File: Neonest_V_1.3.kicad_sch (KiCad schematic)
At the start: 4 parts

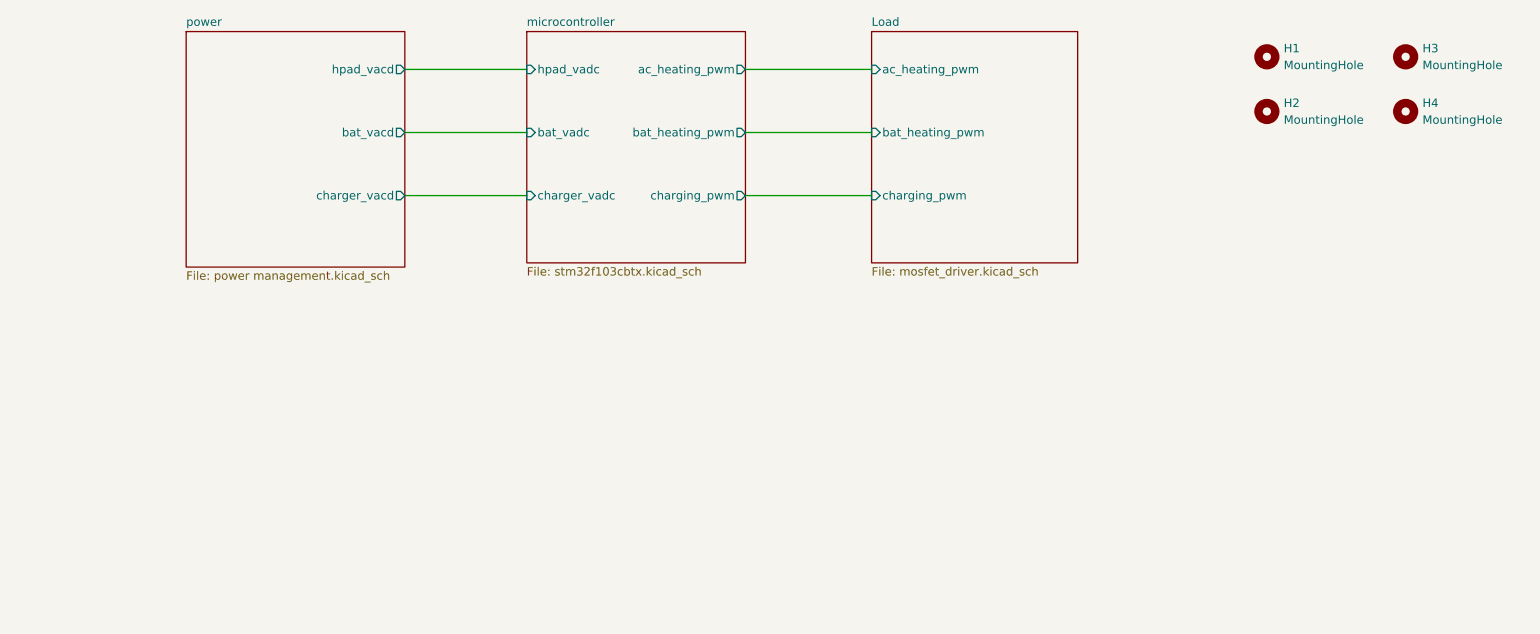
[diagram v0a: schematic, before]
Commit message: Formatted schematic and Increased power tracks
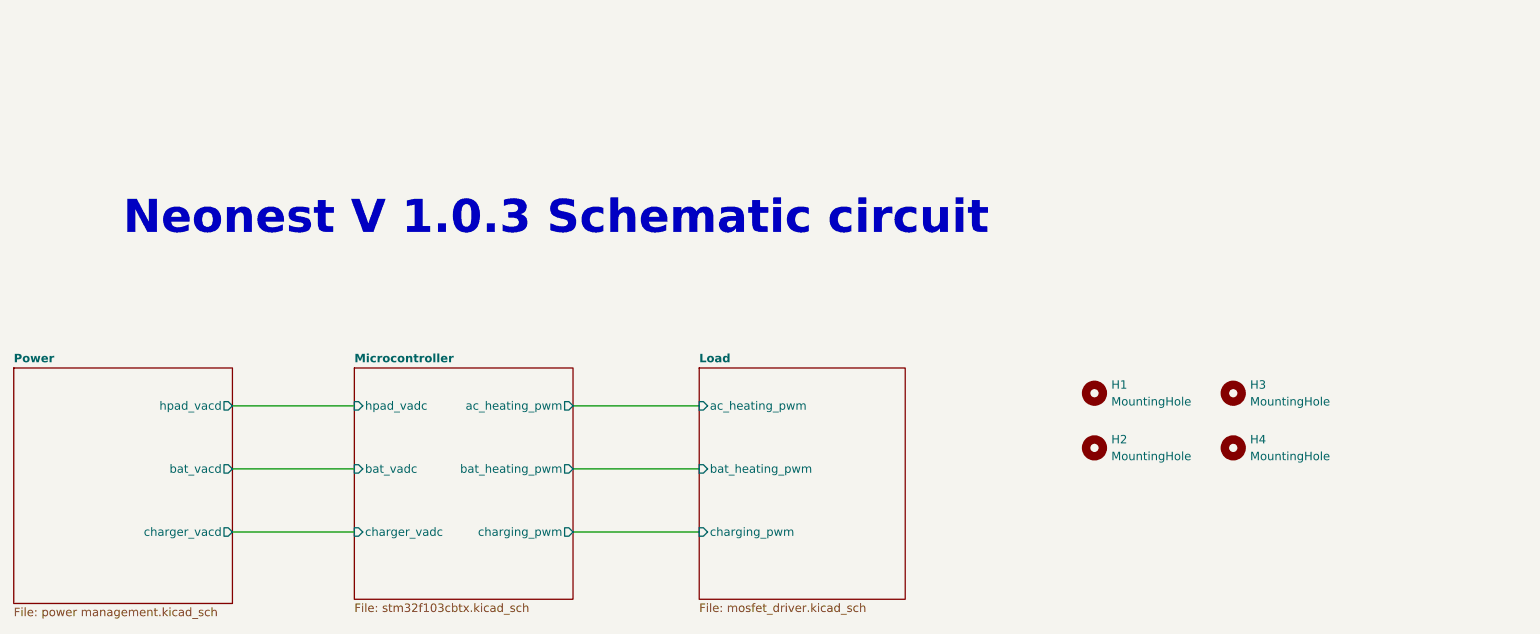
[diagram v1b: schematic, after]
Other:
- sheet microcontroller renamed Microcontroller
- sheet power renamed Power
- note added: "Neonest V 1.0.3 Schematic circuit"
- company: (none) -> Che innovations
- title: (none) -> Neonest v 1.3
- moved on the sheet: H1, H2, H3, H4
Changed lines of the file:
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@@
 (kicad_sch (version 20230121) (generator eeschema)
   (paper "A4")
-  (wire (pts (xy 168.91 43.815) (xy 187.96 43.815))
+  (title_block
+    (title "Neonest v 1.3")
+    (date "2025-08-07")
+    (company "Che innovations")
+  )
+  (wire (pts (xy 142.875 94.615) (xy 161.925 94.615))
     (stroke (width 0) (type default))
   )
-  (wire (pts (xy 117.475 34.29) (xy 135.89 34.29))
+  (wire (pts (xy 91.44 85.09) (xy 109.855 85.09))
     (stroke (width 0) (type default))
   )
-  (wire (pts (xy 117.475 53.34) (xy 135.89 53.34))
+  (wire (pts (xy 91.44 104.14) (xy 109.855 104.14))
     (stroke (width 0) (type default))
   )
-  (wire (pts (xy 168.91 34.29) (xy 187.96 34.29))
+  (wire (pts (xy 142.875 85.09) (xy 161.925 85.09))
     (stroke (width 0) (type default))
   )
-  (wire (pts (xy 168.91 53.34) (xy 187.96 53.34))
+  (wire (pts (xy 142.875 104.14) (xy 161.925 104.14))
     (stroke (width 0) (type default))
   )
-  (wire (pts (xy 117.475 43.815) (xy 135.89 43.815))
+  (wire (pts (xy 91.44 94.615) (xy 109.855 94.615))
     (stroke (width 0) (type default))
   )
-  (symbol (lib_id "Mechanical:MountingHole") (at 268.605 32.385 0) (unit 1)
+  (text "Neonest V 1.0.3 Schematic circuit" (at 74.93 59.69 0)
+    (effects (font (size 5 5) (thickness 1) bold) (justify left bottom))
+  )
+  (symbol (lib_id "Mechanical:MountingHole") (at 242.57 83.185 0) (unit 1)
     (in_bom yes) (on_board yes) (dnp no) (fields_autoplaced)
-    (property "Reference" "H3" (at 271.145 31.115 0)
+    (property "Reference" "H3" (at 245.11 81.915 0)
       (effects (font (size 1.27 1.27)) (justify left))
     )
-    (property "Value" "MountingHole" (at 271.145 33.655 0)
+    (property "Value" "MountingHole" (at 245.11 84.455 0)
       (effects (font (size 1.27 1.27)) (justify left))
     )
-    (property "Footprint" "MountingHole:MountingHole_4mm" (at 268.605 32.385 0)
+    (property "Footprint" "MountingHole:MountingHole_4mm" (at 242.57 83.185 0)
       (effects (font (size 1.27 1.27)) hide)
     )
-    (property "Datasheet" "~" (at 268.605 32.385 0)
+    (property "Datasheet" "~" (at 242.57 83.185 0)
       (effects (font (size 1.27 1.27)) hide)
     )
@@
     )
   )
-  (symbol (lib_id "Mechanical:MountingHole") (at 247.65 40.64 0) (unit 1)
+  (symbol (lib_id "Mechanical:MountingHole") (at 221.615 91.44 0) (unit 1)
     (in_bom yes) (on_board yes) (dnp no) (fields_autoplaced)
-    (property "Reference" "H2" (at 250.19 39.37 0)
+    (property "Reference" "H2" (at 224.155 90.17 0)
       (effects (font (size 1.27 1.27)) (justify left))
     )
-    (property "Value" "MountingHole" (at 250.19 41.91 0)
+    (property "Value" "MountingHole" (at 224.155 92.71 0)
       (effects (font (size 1.27 1.27)) (justify left))
     )
-    (property "Footprint" "MountingHole:MountingHole_4mm" (at 247.65 40.64 0)
+    (property "Footprint" "MountingHole:MountingHole_4mm" (at 221.615 91.44 0)
       (effects (font (size 1.27 1.27)) hide)
     )
-    (property "Datasheet" "~" (at 247.65 40.64 0)
+    (property "Datasheet" "~" (at 221.615 91.44 0)
       (effects (font (size 1.27 1.27)) hide)
     )
@@
     )
   )
-  (symbol (lib_id "Mechanical:MountingHole") (at 247.65 32.385 0) (unit 1)
+  (symbol (lib_id "Mechanical:MountingHole") (at 221.615 83.185 0) (unit 1)
     (in_bom yes) (on_board yes) (dnp no) (fields_autoplaced)
-    (property "Reference" "H1" (at 250.19 31.115 0)
+    (property "Reference" "H1" (at 224.155 81.915 0)
       (effects (font (size 1.27 1.27)) (justify left))
     )
-    (property "Value" "MountingHole" (at 250.19 33.655 0)
+    (property "Value" "MountingHole" (at 224.155 84.455 0)
       (effects (font (size 1.27 1.27)) (justify left))
     )
-    (property "Footprint" "MountingHole:MountingHole_4mm" (at 247.65 32.385 0)
+    (property "Footprint" "MountingHole:MountingHole_4mm" (at 221.615 83.185 0)
       (effects (font (size 1.27 1.27)) hide)
     )
-    (property "Datasheet" "~" (at 247.65 32.385 0)
+    (property "Datasheet" "~" (at 221.615 83.185 0)
       (effects (font (size 1.27 1.27)) hide)
     )
@@
     )
   )
-  (symbol (lib_id "Mechanical:MountingHole") (at 268.605 40.64 0) (unit 1)
+  (symbol (lib_id "Mechanical:MountingHole") (at 242.57 91.44 0) (unit 1)
     (in_bom yes) (on_board yes) (dnp no) (fields_autoplaced)
-    (property "Reference" "H4" (at 271.145 39.37 0)
+    (property "Reference" "H4" (at 245.11 90.17 0)
       (effects (font (size 1.27 1.27)) (justify left))
     )
-    (property "Value" "MountingHole" (at 271.145 41.91 0)
+    (property "Value" "MountingHole" (at 245.11 92.71 0)
       (effects (font (size 1.27 1.27)) (justify left))
     )
-    (property "Footprint" "MountingHole:MountingHole_4mm" (at 268.605 40.64 0)
+    (property "Footprint" "MountingHole:MountingHole_4mm" (at 242.57 91.44 0)
       (effects (font (size 1.27 1.27)) hide)
     )
-    (property "Datasheet" "~" (at 268.605 40.64 0)
+    (property "Datasheet" "~" (at 242.57 91.44 0)
       (effects (font (size 1.27 1.27)) hide)
     )
@@
     )
   )
-  (sheet (at 135.89 28.575) (size 33.02 34.925) (fields_autoplaced)
+  (sheet (at 109.855 79.375) (size 33.02 34.925) (fields_autoplaced)
     (stroke (width 0.1524) (type solid))
     (fill (color 0 0 0 0.0000))
-    (property "Sheetname" "microcontroller" (at 135.89 27.8634 0)
-      (effects (font (size 1.27 1.27)) (justify left bottom))
+    (property "Sheetname" "Microcontroller" (at 109.855 78.6634 0)
+      (effects (font (size 1.27 1.27) bold) (justify left bottom))
     )
-    (property "Sheetfile" "stm32f103cbtx.kicad_sch" (at 135.89 64.0846 0)
+    (property "Sheetfile" "stm32f103cbtx.kicad_sch" (at 109.855 114.8846 0)
       (effects (font (size 1.27 1.27)) (justify left top))
     )
-    (pin "hpad_vadc" input (at 135.89 34.29 180)
+    (pin "hpad_vadc" input (at 109.855 85.09 180)
       (effects (font (size 1.27 1.27)) (justify left))
     )
-    (pin "bat_vadc" input (at 135.89 43.815 180)
+    (pin "bat_vadc" input (at 109.855 94.615 180)
       (effects (font (size 1.27 1.27)) (justify left))
     )
-    (pin "charger_vadc" input (at 135.89 53.34 180)
+    (pin "charger_vadc" input (at 109.855 104.14 180)
       (effects (font (size 1.27 1.27)) (justify left))
     )
-    (pin "ac_heating_pwm" output (at 168.91 34.29 0)
+    (pin "ac_heating_pwm" output (at 142.875 85.09 0)
       (effects (font (size 1.27 1.27)) (justify right))
     )
-    (pin "bat_heating_pwm" output (at 168.91 43.815 0)
+    (pin "bat_heating_pwm" output (at 142.875 94.615 0)
       (effects (font (size 1.27 1.27)) (justify right))
     )
-    (pin "charging_pwm" output (at 168.91 53.34 0)
+    (pin "charging_pwm" output (at 142.875 104.14 0)
       (effects (font (size 1.27 1.27)) (justify right))
     )
@@
     )
   )
-  (sheet (at 187.96 28.575) (size 31.115 34.925) (fields_autoplaced)
+  (sheet (at 161.925 79.375) (size 31.115 34.925) (fields_autoplaced)
     (stroke (width 0.1524) (type solid))
     (fill (color 0 0 0 0.0000))
-    (property "Sheetname" "Load" (at 187.96 27.8634 0)
-      (effects (font (size 1.27 1.27)) (justify left bottom))
+    (property "Sheetname" "Load" (at 161.925 78.6634 0)
+      (effects (font (size 1.27 1.27) bold) (justify left bottom))
     )
-    (property "Sheetfile" "mosfet_driver.kicad_sch" (at 187.96 64.0846 0)
+    (property "Sheetfile" "mosfet_driver.kicad_sch" (at 161.925 114.8846 0)
       (effects (font (size 1.27 1.27)) (justify left top))
     )
-    (pin "bat_heating_pwm" input (at 187.96 43.815 180)
+    (pin "bat_heating_pwm" input (at 161.925 94.615 180)
       (effects (font (size 1.27 1.27)) (justify left))
     )
-    (pin "ac_heating_pwm" input (at 187.96 34.29 180)
+    (pin "ac_heating_pwm" input (at 161.925 85.09 180)
       (effects (font (size 1.27 1.27)) (justify left))
     )
-    (pin "charging_pwm" input (at 187.96 53.34 180)
+    (pin "charging_pwm" input (at 161.925 104.14 180)
       (effects (font (size 1.27 1.27)) (justify left))
     )
@@
     )
   )
-  (sheet (at 84.455 28.575) (size 33.02 35.56) (fields_autoplaced)
+  (sheet (at 58.42 79.375) (size 33.02 35.56) (fields_autoplaced)
     (stroke (width 0.1524) (type solid))
     (fill (color 0 0 0 0.0000))
-    (property "Sheetname" "power" (at 84.455 27.8634 0)
-      (effects (font (size 1.27 1.27)) (justify left bottom))
+    (property "Sheetname" "Power" (at 58.42 78.6634 0)
+      (effects (font (size 1.27 1.27) bold) (justify left bottom))
     )
-    (property "Sheetfile" "power management.kicad_sch" (at 84.455 64.7196 0)
+    (property "Sheetfile" "power management.kicad_sch" (at 58.42 115.5196 0)
       (effects (font (size 1.27 1.27)) (justify left top))
     )
-    (pin "bat_vacd" output (at 117.475 43.815 0)
+    (pin "bat_vacd" output (at 91.44 94.615 0)
       (effects (font (size 1.27 1.27)) (justify right))
     )
-    (pin "charger_vacd" output (at 117.475 53.34 0)
+    (pin "charger_vacd" output (at 91.44 104.14 0)
       (effects (font (size 1.27 1.27)) (justify right))
     )
-    (pin "hpad_vacd" output (at 117.475 34.29 0)
+    (pin "hpad_vacd" output (at 91.44 85.09 0)
       (effects (font (size 1.27 1.27)) (justify right))
     )
